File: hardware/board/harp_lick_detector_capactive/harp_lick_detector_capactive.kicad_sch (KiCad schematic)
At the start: 23 parts, among them J5 Barrel_Jack_Switch, U5 LT3030, U6 LM27762

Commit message: update bandpass filter; plan pico shield version
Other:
- note added: "TODO: raw signal out for debugging."
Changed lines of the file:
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@@
+    (effects (font (size 1.27 1.27)) (justify left bottom))
+  )
+  (text "TODO: raw signal out for debugging." (at 115.57 83.82 0)
     (effects (font (size 1.27 1.27)) (justify left bottom))
   )
@@
       (reference "#PWR0145") (unit 1) (value "GNDA") (footprint "")
     )
-    (path "/faa455ea-93b0-4a12-9af2-c32e7eee6d37/647e764a-2812-4470-a9a2-62513d3d17e7"
-      (reference "#PWR0146") (unit 1) (value "GND") (footprint "")
-    )
     (path "/faa455ea-93b0-4a12-9af2-c32e7eee6d37/9cf01063-f90b-432e-9e9a-422c494cd3c3"

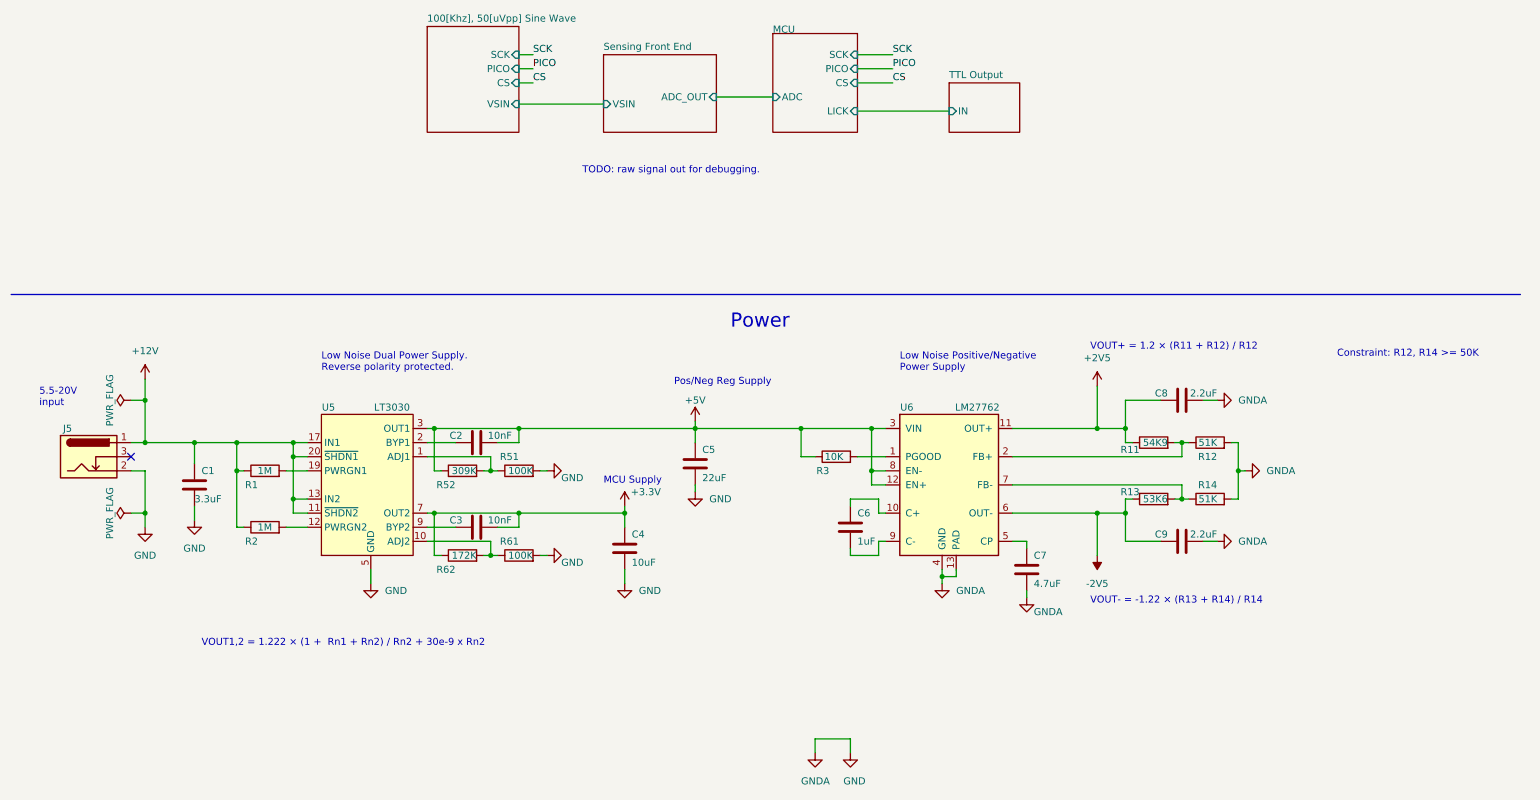
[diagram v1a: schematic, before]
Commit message: draft ads7029 pio driver
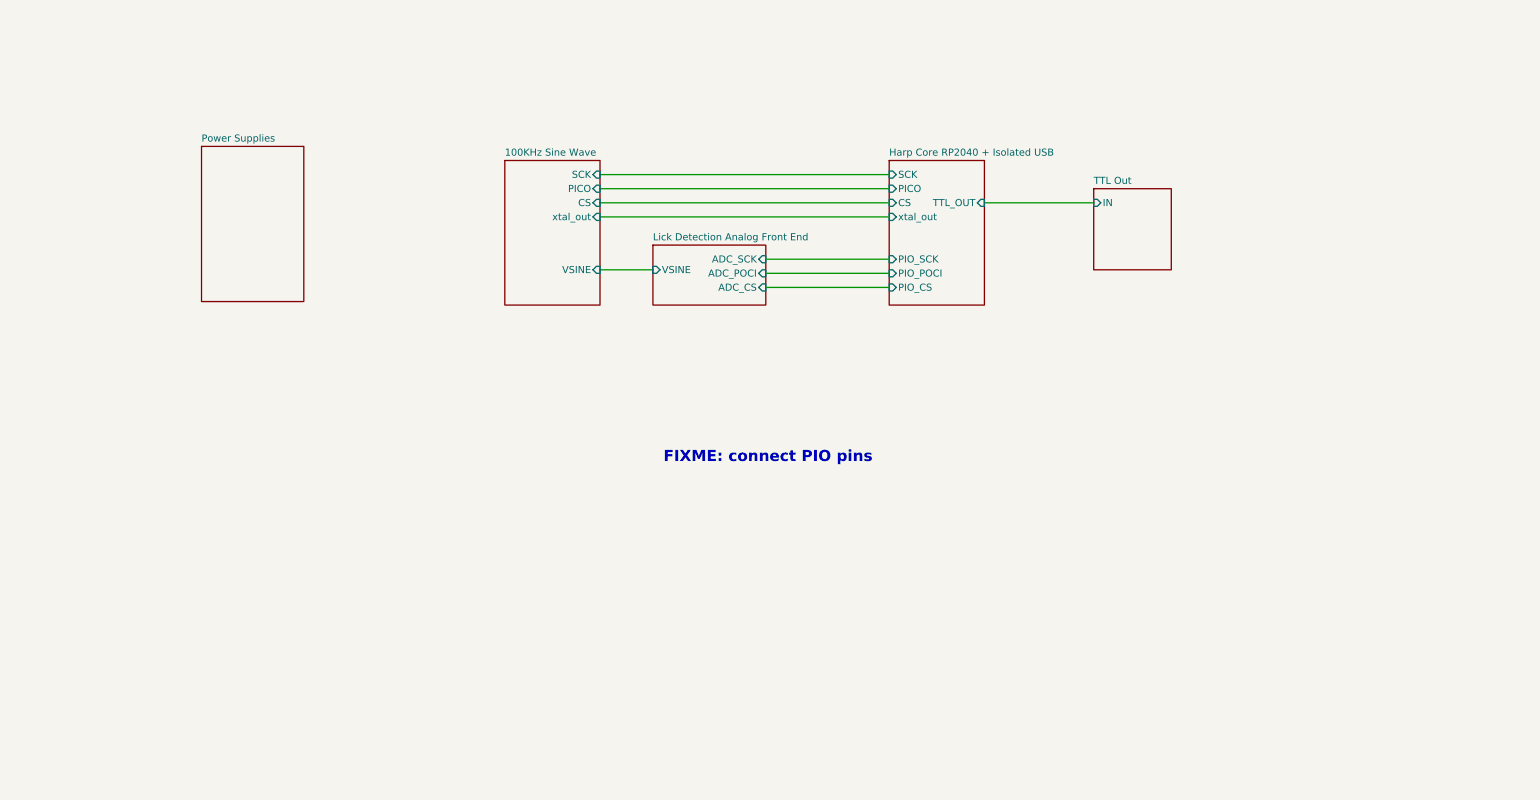
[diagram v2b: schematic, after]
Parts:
- removed C1: 3.3uF, Capacitor_SMD:C_0805_2012Metric_Pad1.18x1.45mm_HandSolder, symbol Device:C
- removed C2, C3: 10nF, Capacitor_SMD:C_0603_1608Metric_Pad1.08x0.95mm_HandSolder, symbol Device:C
- removed C4: 10uF, Capacitor_SMD:C_0805_2012Metric, symbol Device:C
- removed C5: 22uF, Capacitor_SMD:C_0805_2012Metric, symbol Device:C
- removed C6: 1uF, Capacitor_SMD:C_0603_1608Metric_Pad1.08x0.95mm_HandSolder, symbol Device:C
- removed C7: 4.7uF, Capacitor_SMD:C_0805_2012Metric_Pad1.18x1.45mm_HandSolder, symbol Device:C
- removed C8, C9: 2.2uF, Capacitor_SMD:C_0603_1608Metric_Pad1.08x0.95mm_HandSolder, symbol Device:C
- removed J5: Barrel_Jack_Switch, Connector_BarrelJack:BarrelJack_CUI_PJ-036AH-SMT_Horizontal, symbol Connector:Barrel_Jack_Switch
- removed R1, R2: 1M, Resistor_SMD:R_0603_1608Metric_Pad0.98x0.95mm_HandSolder, symbol Device:R
- removed R11: 54K9, Resistor_SMD:R_0603_1608Metric_Pad0.98x0.95mm_HandSolder, symbol Device:R
- removed R12, R14: 51K, Resistor_SMD:R_0603_1608Metric_Pad0.98x0.95mm_HandSolder, symbol Device:R
- removed R13: 53K6, Resistor_SMD:R_0603_1608Metric_Pad0.98x0.95mm_HandSolder, symbol Device:R
- removed R3: 10K, Resistor_SMD:R_0402_1005Metric_Pad0.72x0.64mm_HandSolder, symbol Device:R
- removed R51, R61: 100K, Resistor_SMD:R_0603_1608Metric_Pad0.98x0.95mm_HandSolder, symbol Device:R
- removed R52: 309K, Resistor_SMD:R_0603_1608Metric_Pad0.98x0.95mm_HandSolder, symbol Device:R
- removed R62: 172K, Resistor_SMD:R_0603_1608Metric_Pad0.98x0.95mm_HandSolder, symbol Device:R
- removed U5: LT3030, Package_SO:ETSSOP-20-1EP_4.4x6.5mm_P0.65mm_EP3x4.2mm, symbol machine_agency_components:LT3030
- removed U6: LM27762, Package_SON:WSON-12-1EP_3x2mm_P0.5mm_EP1x2.65_ThermalVias, symbol Regulator_SwitchedCapacitor:LM27762
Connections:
- no-connect marks 1 -> 0
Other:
- removed sheet 100[Khz], 50[uVpp] Sine Wave
- removed sheet MCU
- removed sheet Sensing Front End
- removed sheet TTL Output
- added sheet 100KHz Sine Wave (function_generator.kicad_sch)
- added sheet Harp Core RP2040 + Isolated USB (isolated_usb_rp2040.kicad_sch)
- added sheet Lick Detection Analog Front End (lick_detection_afe.kicad_sch)
- added sheet Power Supplies (board_power.kicad_sch)
- added sheet TTL Out (sma_ttl_out.kicad_sch)
- note added: "FIXME: connect PIO pins"
- note removed: "5.5-20V input"
- note removed: "Constraint: R12, R14 >= 50K"
- note removed: "Low Noise Dual Power Supply. Reverse polarity protected."
- note removed: "Low Noise Positive/Negative Power Supply"
- note removed: "MCU Supply"
- note removed: "Pos/Neg Reg Supply"
- note removed: "Power"
- note removed: "TODO: raw signal out for debugging."
- note removed: "VOUT+ = 1.2 × (R11 + R12) / R12"
- note removed: "VOUT- = -1.22 × (R13 + R14) / R14"
- note removed: "VOUT1,2 = 1.222 × (1 + Rn1 + Rn2) / Rn2 + 30e-9 x Rn2"

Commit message: draft consolidated board
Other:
- sheet 100KHz Sine Wave ports: added xtal_in; removed xtal_out
- note removed: "FIXME: connect PIO pins"
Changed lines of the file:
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@@
     (stroke (width 0) (type default))
-  )
-  (text "FIXME: connect PIO pins" (at 130.175 135.89 0)
-    (effects (font (size 2 2) (thickness 0.4) bold) (justify left bottom))
   )
   (sheet (at 207.645 86.36) (size 13.97 14.605) (fields_autoplaced)
@@
       (effects (font (size 1.27 1.27)) (justify right))
     )
-    (pin "xtal_out" input (at 118.745 91.44 0)
+    (pin "xtal_in" input (at 118.745 91.44 0)
       (effects (font (size 1.27 1.27)) (justify right))
     )

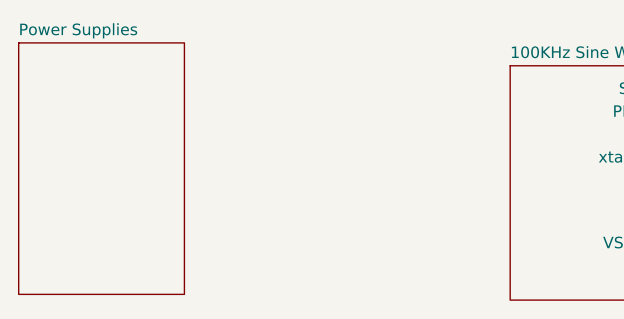
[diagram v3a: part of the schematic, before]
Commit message: remove hand-soldering footprints
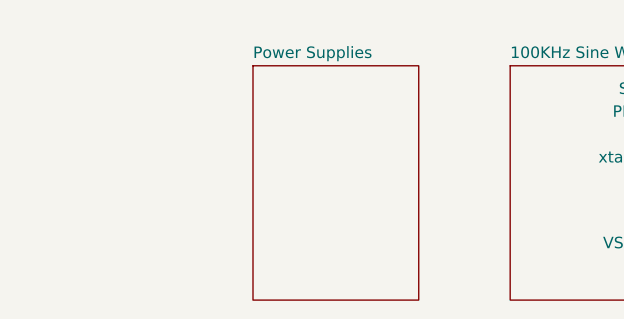
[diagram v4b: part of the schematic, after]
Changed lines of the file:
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@@
     )
   )
-  (sheet (at 46.99 78.74) (size 18.415 27.94) (fields_autoplaced)
+  (sheet (at 73.025 81.28) (size 18.415 26.035) (fields_autoplaced)
     (stroke (width 0.1524) (type solid))
     (fill (color 0 0 0 0.0000))
-    (property "Sheetname" "Power Supplies" (at 46.99 78.0284 0)
+    (property "Sheetname" "Power Supplies" (at 73.025 80.5684 0)
       (effects (font (size 1.27 1.27)) (justify left bottom))
     )
-    (property "Sheetfile" "board_power.kicad_sch" (at 46.99 107.2646 0)
+    (property "Sheetfile" "board_power.kicad_sch" (at 73.025 107.8996 0)
       (effects (font (size 1.27 1.27)) (justify left top) hide)
     )

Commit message: update footprints; populate bom
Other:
- company: (none) -> The Allen Institute for Neural Dynamics
- title: (none) -> Lickety Split Capacitive Lick Detector
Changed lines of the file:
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@@
 (kicad_sch (version 20230121) (generator eeschema)
   (paper "A4")
+  (title_block
+    (title "Lickety Split Capacitive Lick Detector")
+    (date "2023-09-01")
+    (rev "0.5")
+    (company "The Allen Institute for Neural Dynamics")
+  )
   (wire (pts (xy 118.745 83.82) (xy 170.815 83.82))
     (stroke (width 0) (type default))

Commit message: draft v0.6.0 board
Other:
- sheet 100KHz Sine Wave ports: added 100KHZ_SQ_WAVE_IN; removed CS, PICO, SCK, xtal_in
- sheet Harp Core RP2040 + Isolated USB ports: added 100KHZ_SQ_WAVE_OUT; removed CS, PICO, SCK, xtal_out
- note added: "DONE: change J1 COAX signal probe to hook DONE: update bandpass filter to 4th order. U6B and U6D should be used as stage 1 and 2. DONE: increase R42, R43 to reduce the effect of the transient. ~64 ohms each is safe for 2MHz sampling. Higher would be better. DONE: consolidate U6C and U6D into one op-amp that handles gain and offset in a single stage w/100x amplification. DONE: use REF2033 (dual: 1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"
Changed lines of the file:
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@@
     (title "Lickety Split Capacitive Lick Detector")
     (date "2023-09-01")
-    (rev "0.5")
+    (rev "0.6")
     (company "The Allen Institute for Neural Dynamics")
   )
-  (wire (pts (xy 118.745 83.82) (xy 170.815 83.82))
+  (wire (pts (xy 118.745 100.965) (xy 133.35 100.965))
     (stroke (width 0) (type default))
   )
-  (wire (pts (xy 118.745 100.965) (xy 128.27 100.965))
+  (wire (pts (xy 153.67 104.14) (xy 169.545 104.14))
     (stroke (width 0) (type default))
   )
-  (wire (pts (xy 148.59 104.14) (xy 170.815 104.14))
+  (wire (pts (xy 195.58 90.17) (xy 207.645 90.17))
     (stroke (width 0) (type default))
   )
-  (wire (pts (xy 187.96 88.9) (xy 207.645 88.9))
+  (wire (pts (xy 153.67 101.6) (xy 169.545 101.6))
     (stroke (width 0) (type default))
   )
-  (wire (pts (xy 118.745 88.9) (xy 170.815 88.9))
+  (wire (pts (xy 153.67 99.06) (xy 169.545 99.06))
     (stroke (width 0) (type default))
   )
-  (wire (pts (xy 148.59 101.6) (xy 170.815 101.6))
+  (wire (pts (xy 118.745 85.725) (xy 169.545 85.725))
     (stroke (width 0) (type default))
   )
-  (wire (pts (xy 118.745 86.36) (xy 170.815 86.36))
-    (stroke (width 0) (type default))
-  )
-  (wire (pts (xy 148.59 99.06) (xy 170.815 99.06))
-    (stroke (width 0) (type default))
-  )
-  (wire (pts (xy 118.745 91.44) (xy 170.815 91.44))
-    (stroke (width 0) (type default))
+  (text "DONE: change J1 COAX signal probe to hook\nDONE: update bandpass filter to 4th order. U6B and U6D should be used as stage 1 and 2.\nDONE: increase R42, R43 to reduce the effect of the transient. \n    ~64 ohms each is safe for 2MHz sampling. Higher would be better.\nDONE: consolidate U6C and U6D into one op-amp that handles gain and offset in a single stage w/100x amplification.\nDONE: use REF2033 (dual: 1.65V, 3.3V) reference voltage output\nDONE: replace DDS chip with filtered square wave.\nDONE: update Bootsel button with aqueous wash-compatible version."
+    (at 99.695 139.7 0)
+    (effects (font (size 1.27 1.27)) (justify left bottom))
   )
   (sheet (at 207.645 86.36) (size 13.97 14.605) (fields_autoplaced)
@@
       (effects (font (size 1.27 1.27)) (justify left top) hide)
     )
-    (pin "IN" input (at 207.645 88.9 180)
+    (pin "IN" input (at 207.645 90.17 180)
       (effects (font (size 1.27 1.27)) (justify left))
     )
@@
     )
   )
-  (sheet (at 101.6 81.28) (size 17.145 26.035) (fields_autoplaced)
+  (sheet (at 94.615 81.28) (size 24.13 26.035) (fields_autoplaced)
     (stroke (width 0.1524) (type solid))
     (fill (color 0 0 0 0.0000))
-    (property "Sheetname" "100KHz Sine Wave" (at 101.6 80.5684 0)
+    (property "Sheetname" "100KHz Sine Wave" (at 94.615 80.5684 0)
       (effects (font (size 1.27 1.27)) (justify left bottom))
     )
-    (property "Sheetfile" "function_generator.kicad_sch" (at 101.6 107.8996 0)
+    (property "Sheetfile" "function_generator.kicad_sch" (at 94.615 107.8996 0)
       (effects (font (size 1.27 1.27)) (justify left top) hide)
-    )
-    (pin "PICO" input (at 118.745 86.36 0)
-      (effects (font (size 1.27 1.27)) (justify right))
-    )
-    (pin "SCK" input (at 118.745 83.82 0)
-      (effects (font (size 1.27 1.27)) (justify right))
-    )
-    (pin "CS" input (at 118.745 88.9 0)
-      (effects (font (size 1.27 1.27)) (justify right))
     )
     (pin "VSINE" input (at 118.745 100.965 0)
       (effects (font (size 1.27 1.27)) (justify right))
     )
-    (pin "xtal_in" input (at 118.745 91.44 0)
+    (pin "100KHZ_SQ_WAVE_IN" input (at 118.745 85.725 0)
       (effects (font (size 1.27 1.27)) (justify right))
     )
@@
     )
   )
-  (sheet (at 128.27 96.52) (size 20.32 10.795) (fields_autoplaced)
+  (sheet (at 133.35 95.25) (size 20.32 12.065) (fields_autoplaced)
     (stroke (width 0.1524) (type solid))
     (fill (color 0 0 0 0.0000))
-    (property "Sheetname" "Lick Detection Analog Front End" (at 128.27 95.8084 0)
+    (property "Sheetname" "Lick Detection Analog Front End" (at 133.35 94.5384 0)
       (effects (font (size 1.27 1.27)) (justify left bottom))
     )
-    (property "Sheetfile" "lick_detection_afe.kicad_sch" (at 128.27 107.8996 0)
+    (property "Sheetfile" "lick_detection_afe.kicad_sch" (at 133.35 107.8996 0)
       (effects (font (size 1.27 1.27)) (justify left top) hide)
     )
-    (pin "VSINE" input (at 128.27 100.965 180)
+    (pin "VSINE" input (at 133.35 100.965 180)
       (effects (font (size 1.27 1.27)) (justify left))
     )
-    (pin "ADC_SCK" input (at 148.59 99.06 0)
+    (pin "ADC_SCK" input (at 153.67 99.06 0)
       (effects (font (size 1.27 1.27)) (justify right))
     )
-    (pin "ADC_CS" input (at 148.59 104.14 0)
+    (pin "ADC_CS" input (at 153.67 104.14 0)
       (effects (font (size 1.27 1.27)) (justify right))
     )
-    (pin "ADC_POCI" input (at 148.59 101.6 0)
+    (pin "ADC_POCI" input (at 153.67 101.6 0)
       (effects (font (size 1.27 1.27)) (justify right))
     )
@@
     )
   )
-  (sheet (at 73.025 81.28) (size 18.415 26.035) (fields_autoplaced)
+  (sheet (at 64.77 81.28) (size 18.415 26.035) (fields_autoplaced)
     (stroke (width 0.1524) (type solid))
     (fill (color 0 0 0 0.0000))
-    (property "Sheetname" "Power Supplies" (at 73.025 80.5684 0)
+    (property "Sheetname" "Power Supplies" (at 64.77 80.5684 0)
       (effects (font (size 1.27 1.27)) (justify left bottom))
     )
-    (property "Sheetfile" "board_power.kicad_sch" (at 73.025 107.8996 0)
+    (property "Sheetfile" "board_power.kicad_sch" (at 64.77 107.8996 0)
       (effects (font (size 1.27 1.27)) (justify left top) hide)
     )
@@
     )
   )
-  (sheet (at 170.815 81.28) (size 17.145 26.035) (fields_autoplaced)
+  (sheet (at 169.545 81.28) (size 26.035 26.035) (fields_autoplaced)
     (stroke (width 0.1524) (type solid))
     (fill (color 0 0 0 0.0000))
-    (property "Sheetname" "Harp Core RP2040 + Isolated USB" (at 170.815 80.5684 0)
+    (property "Sheetname" "Harp Core RP2040 + Isolated USB" (at 169.545 80.5684 0)
       (effects (font (size 1.27 1.27)) (justify left bottom))
     )
-    (property "Sheetfile" "isolated_usb_rp2040.kicad_sch" (at 170.815 107.8996 0)
+    (property "Sheetfile" "isolated_usb_rp2040.kicad_sch" (at 169.545 107.8996 0)
       (effects (font (size 1.27 1.27)) (justify left top) hide)
     )
-    (pin "SCK" input (at 170.815 83.82 180)
+    (pin "TTL_OUT" input (at 195.58 90.17 0)
+      (effects (font (size 1.27 1.27)) (justify right))
+    )
+    (pin "PIO_SCK" input (at 169.545 99.06 180)
       (effects (font (size 1.27 1.27)) (justify left))
     )
-    (pin "CS" input (at 170.815 88.9 180)
+    (pin "PIO_POCI" input (at 169.545 101.6 180)
       (effects (font (size 1.27 1.27)) (justify left))
     )
-    (pin "PICO" input (at 170.815 86.36 180)
+    (pin "PIO_CS" input (at 169.545 104.14 180)
       (effects (font (size 1.27 1.27)) (justify left))
     )
-    (pin "TTL_OUT" input (at 187.96 88.9 0)
-      (effects (font (size 1.27 1.27)) (justify right))
-    )
-    (pin "PIO_SCK" input (at 170.815 99.06 180)
+    (pin "100KHZ_SQ_WAVE_OUT" input (at 169.545 85.725 180)
       (effects (font (size 1.27 1.27)) (justify left))
     )
-    (pin "PIO_POCI" input (at 170.815 101.6 180)
-      (effects (font (size 1.27 1.27)) (justify left))
-    )
-    (pin "PIO_CS" input (at 170.815 104.14 180)
-      (effects (font (size 1.27 1.27)) (justify left))
-    )
-    (pin "xtal_out" input (at 170.815 91.44 180)
-      (effects (font (size 1.27 1.27)) (justify left))
-    )

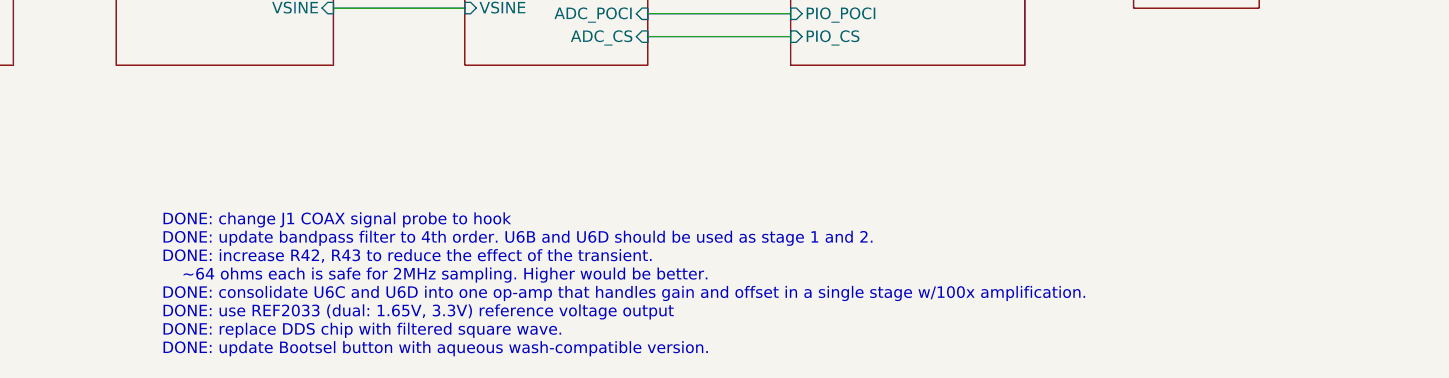
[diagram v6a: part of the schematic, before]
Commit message: remove extraneous schematic notes
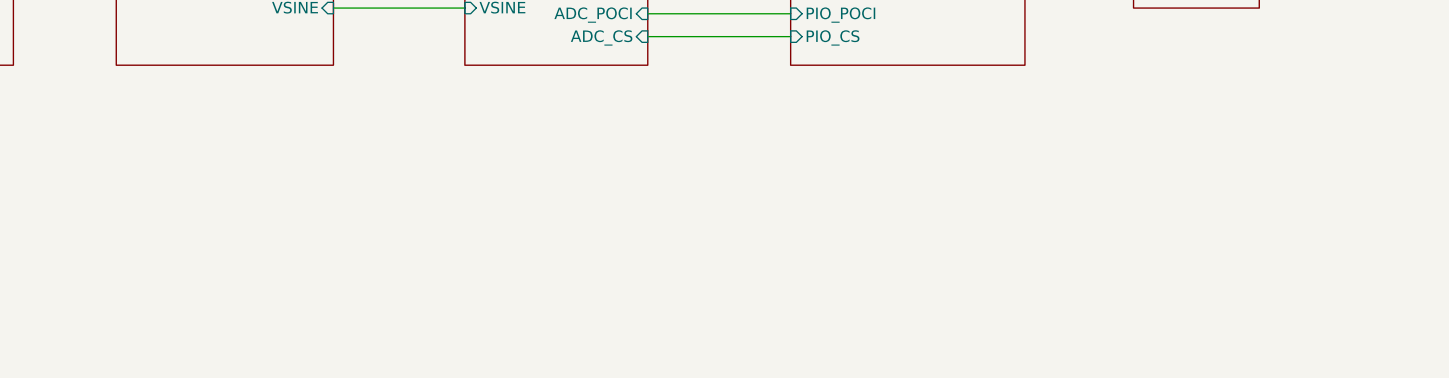
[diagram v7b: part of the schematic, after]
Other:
- note removed: "DONE: change J1 COAX signal probe to hook DONE: update bandpass filter to 4th order. U6B and U6D should be used as stage 1 and 2. DONE: increase R42, R43 to reduce the effect of the transient. ~64 ohms each is safe for 2MHz sampling. Higher would be better. DONE: consolidate U6C and U6D into one op-amp that handles gain and offset in a single stage w/100x amplification. DONE: use REF2033 (dual: 1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"
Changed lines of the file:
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@@
     (stroke (width 0) (type default))
-  )
-  (text "DONE: change J1 COAX signal probe to hook\nDONE: update bandpass filter to 4th order. U6B and U6D should be used as stage 1 and 2.\nDONE: increase R42, R43 to reduce the effect of the transient. \n    ~64 ohms each is safe for 2MHz sampling. Higher would be better.\nDONE: consolidate U6C and U6D into one op-amp that handles gain and offset in a single stage w/100x amplification.\nDONE: use REF2033 (dual: 1.65V, 3.3V) reference voltage output\nDONE: replace DDS chip with filtered square wave.\nDONE: update Bootsel button with aqueous wash-compatible version."
-    (at 99.695 139.7 0)
-    (effects (font (size 1.27 1.27)) (justify left bottom))
   )
   (sheet (at 207.645 86.36) (size 13.97 14.605) (fields_autoplaced)
